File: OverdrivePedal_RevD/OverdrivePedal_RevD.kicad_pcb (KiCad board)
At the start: 2 copper layers, 42.5 x 30.5 mm, 54 parts, among them J1 AudioJack2-Connector, J2 Barrel_Jack, J3 Conn_01x05, J4 SW_SPST, J6 AudioJack2-Connector, U1 DG468DV_T1_E3, U10 PAM2812, U12 DG468DV_T1_E3, U2 TL071, U3 TPS60400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

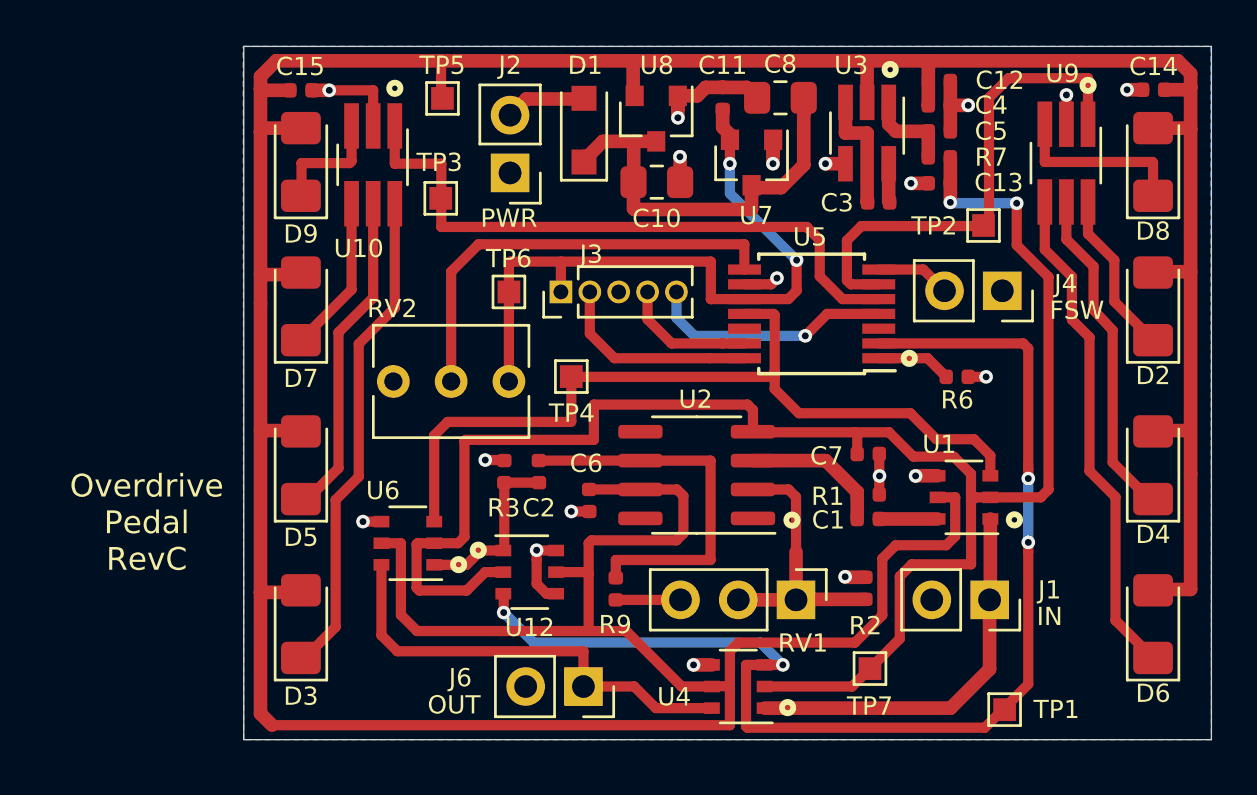
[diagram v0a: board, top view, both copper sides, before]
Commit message: Modified RevD design to use IM43 Relay instead of DG468 SW
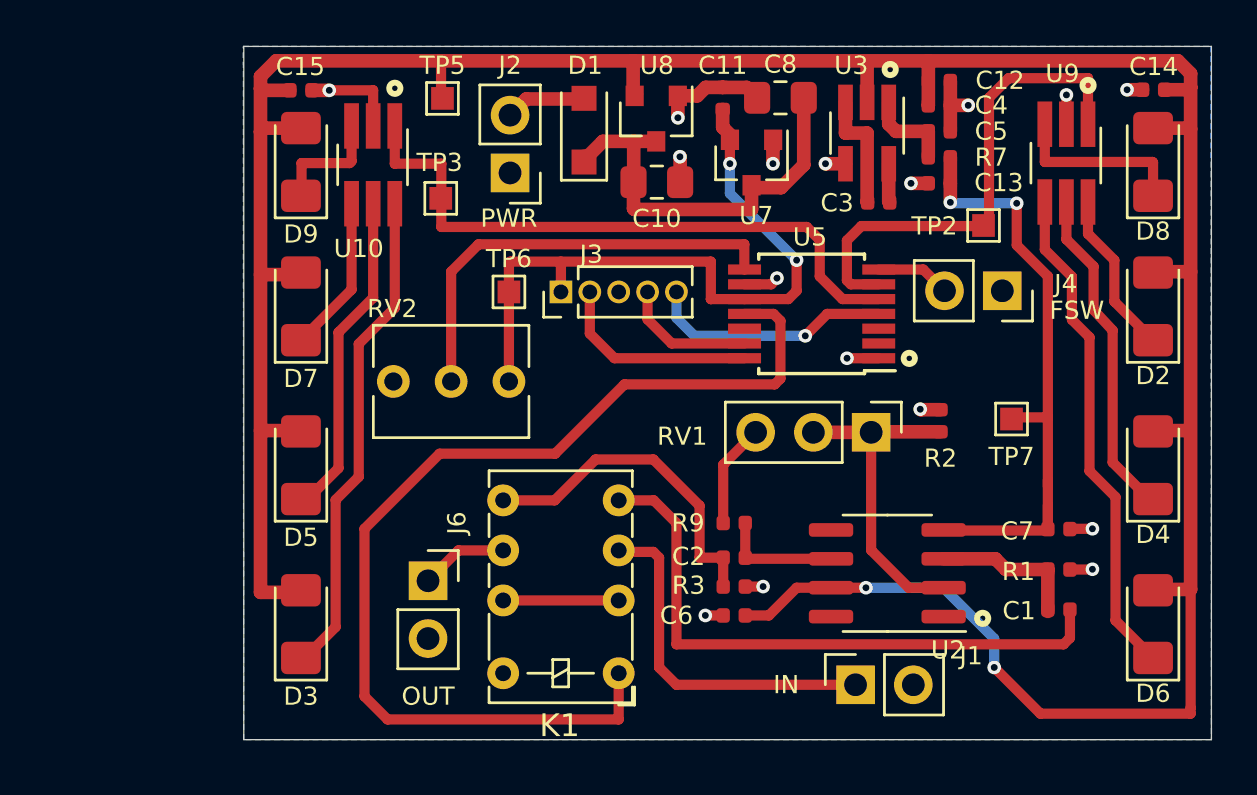
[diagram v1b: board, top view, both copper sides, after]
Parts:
- removed R6: 10K, Resistor_SMD:R_0402_1005Metric
- removed TP1, TP4: TestPoint, TestPoint:TestPoint_Pad_1.0x1.0mm
- removed U1, U12, U4, U6: DG468DV_T1_E3, Package_SO:TSOP-6_1.65x3.05mm_P0.95mm
- added K1: IM43, Relay_THT:Relay_DPDT_AXICOM_IMSeries_Pitch5.08mm, F.Cu at (139.7, 108.2)
- moved TP7 12.6 mm to (157.0, 97.0)
- moved R3 11.3 mm to (144.8, 104.4), turned to 0 degrees
- moved U2 9.43 mm to (151.5, 103.8)
- moved C2 9.38 mm to (144.8, 103.1), turned to 0 degrees
- moved C1 9.28 mm to (159.1, 105.4)
- moved R1 9.01 mm to (159.1, 103.6)
- moved C7 9.01 mm to (159.1, 101.9)
- moved J6 8.26 mm to (131.3, 104.1), turned to 0 degrees
- moved C6 8.14 mm to (144.8, 105.7), turned to 180 degrees
- moved R2 8.07 mm to (153.8, 97.1)
- moved RV1 8.07 mm to (150.8, 97.6)
- moved J1 6.98 mm to (150.1, 108.7), turned to 90 degrees
- moved R9 5.96 mm to (144.8, 101.6), turned to 180 degrees
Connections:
- net Net-(C2-Pad1) renamed /FX_OUT
- C1 pad 2: Net-(C1-Pad2) -> /FX_IN
- J1 pad 1: Net-(J1-Pad1) -> /SIGNAL_IN
- J6 pad 1: Net-(J6-Pad1) -> /SIGNAL_OUT
- U5 pad 1: Net-(R6-Pad2) -> GNDS
- U5 pad 2: /CLEAN_ENABLE -> Net-(U5-Pad2)
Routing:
- net /CLEAN_ENABLE: track 53.1 -> 0.00 mm, vias 4 -> 0
- net +5V: track 190.7 -> 138.5 mm, vias 0 -> 2
- net -5V: track 77.8 -> 27.4 mm
- net /FX_IN: track 0.00 -> 26.9 mm
- net Net-(J6-Pad1): track 19.9 -> 0.00 mm
- net Net-(J1-Pad1): track 17.2 -> 0.00 mm
- net /SIGNAL_IN: track 0.00 -> 15.7 mm
- net Net-(C2-Pad2): track 16.9 -> 5.35 mm
- net /FX_ENABLE: track 37.4 -> 46.3 mm
- net /FX_OUT: track 7.74 -> 14.8 mm
- net GNDS: track 30.1 -> 24.9 mm, vias 19 -> 16
- net /BYPASS: track 0.00 -> 5.08 mm
- net /SIGNAL_OUT: track 0.00 -> 3.86 mm
- net Net-(R6-Pad2): track 3.30 -> 0.00 mm
- net Net-(C1-Pad2): track 2.56 -> 0.00 mm
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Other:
- board text removed: "Overdrive Pedal RevC"
